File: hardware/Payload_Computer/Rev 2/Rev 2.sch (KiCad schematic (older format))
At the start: 0 parts

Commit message: Added Voltage Regulator
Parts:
- added H101: Center_Hole, Rev 2:Center_hole, symbol Rev2symbols:Center_Hole
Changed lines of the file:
@@
 $Descr A4 11693 8268
 encoding utf-8
-Sheet 1 2
+Sheet 1 3
 Title ""
 Date ""
@@
 F1 "TEENSY3.sch" 50
 $EndSheet
+$Comp
+L Rev2symbols:Center_Hole H101
+U 1 1 60565948
+P 5600 5650
+F 0 "H101" H 5678 5696 50  0000 L CNN
+F 1 "Center_Hole" H 5678 5605 50  0000 L CNN
+F 2 "Rev 2:Center_hole" H 5600 5650 50  0001 C CNN
+F 3 "" H 5600 5650 50  0001 C CNN
+	1    5600 5650
+	1    0    0    -1
+$EndComp
+$Sheet
+S 1050 900  1200 650
+U 60566AAD
+F0 "POWER REGULATION" 50
+F1 "POWER REGULATION.sch" 50
+$EndSheet
 $EndSCHEMATC

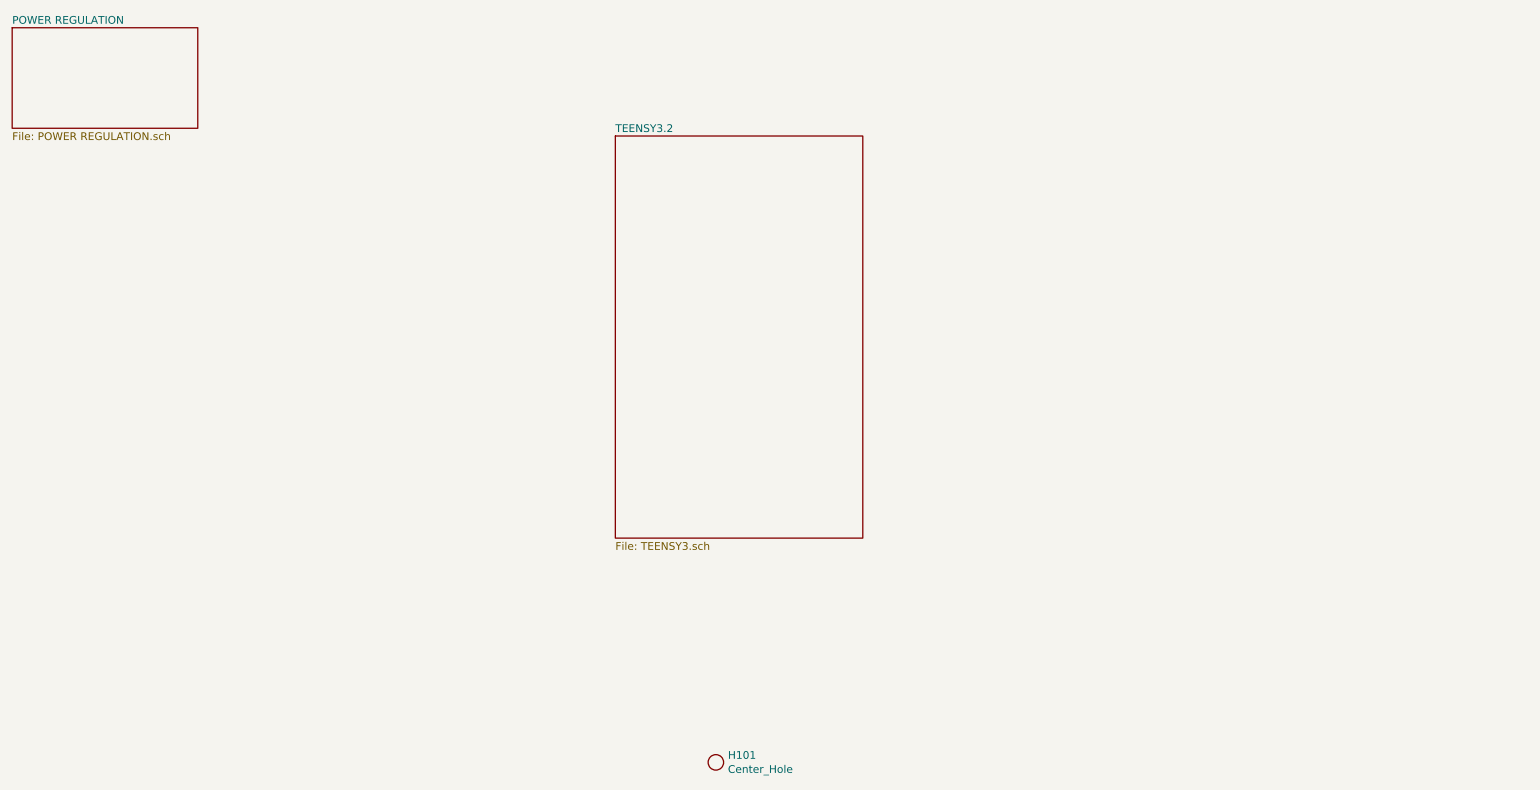
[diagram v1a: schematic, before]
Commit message: More routing and added BNO055
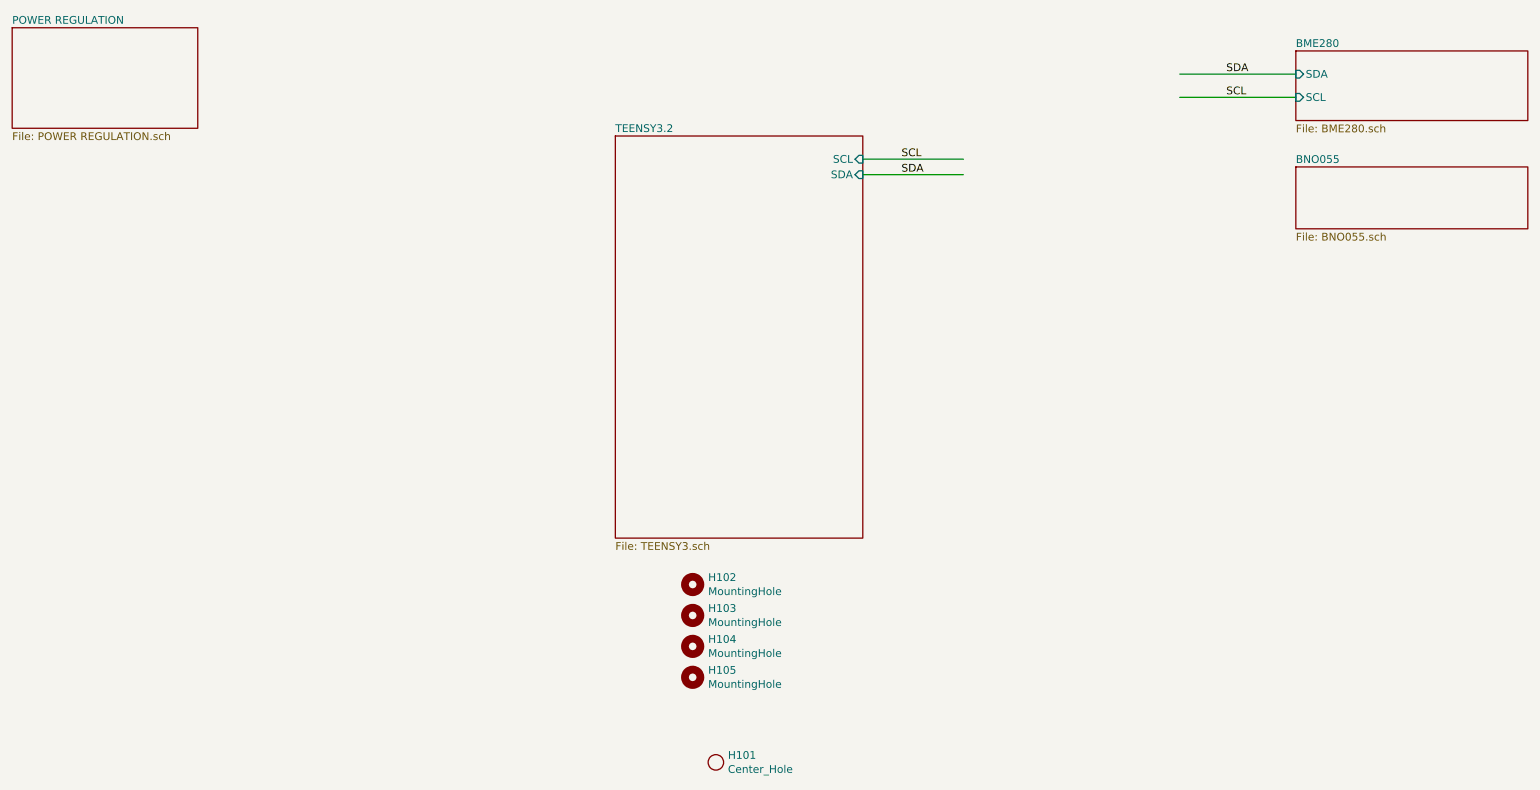
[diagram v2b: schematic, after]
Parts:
- added H102, H103, H104, H105: MountingHole, MountingHole:MountingHole_3.5mm, symbol Mechanical:MountingHole
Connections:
- net labels added: SCL, SDA
- wire segments 0 -> 4
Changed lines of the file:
@@
 $Descr A4 11693 8268
 encoding utf-8
-Sheet 1 3
+Sheet 1 5
 Title ""
 Date ""
@@
 F0 "TEENSY3.2" 50
 F1 "TEENSY3.sch" 50
+F2 "SCL" I R 6550 1750 50
+F3 "SDA" I R 6550 1850 50
 $EndSheet
 $Comp
@@
 F1 "POWER REGULATION.sch" 50
 $EndSheet
+$Sheet
+S 9350 1050 1500 450
+U 60605BA4
+F0 "BME280" 50
+F1 "BME280.sch" 50
+F2 "SDA" I L 9350 1200 50
+F3 "SCL" I L 9350 1350 50
+$EndSheet
+Wire Wire Line
+	9350 1200 8600 1200
+Wire Wire Line
+	9350 1350 8600 1350
+Text Label 8900 1200 0    50   ~ 0
+SDA
+Text Label 8900 1350 0    50   ~ 0
+SCL
+Wire Wire Line
+	6550 1750 7200 1750
+Wire Wire Line
+	6550 1850 7200 1850
+Text Label 6800 1750 0    50   ~ 0
+SCL
+Text Label 6800 1850 0    50   ~ 0
+SDA
+$Sheet
+S 9350 1800 1500 400
+U 6060BC6F
+F0 "BNO055" 50
+F1 "BNO055.sch" 50
+$EndSheet
+$Comp
+L Mechanical:MountingHole H105
+U 1 1 606125CD
+P 5450 5100
+F 0 "H105" H 5550 5146 50  0000 L CNN
+F 1 "MountingHole" H 5550 5055 50  0000 L CNN
+F 2 "MountingHole:MountingHole_3.5mm" H 5450 5100 50  0001 C CNN
+F 3 "~" H 5450 5100 50  0001 C CNN
+	1    5450 5100
+	1    0    0    -1
+$EndComp
+$Comp
+L Mechanical:MountingHole H104
+U 1 1 60612A94
+P 5450 4900
+F 0 "H104" H 5550 4946 50  0000 L CNN
+F 1 "MountingHole" H 5550 4855 50  0000 L CNN
+F 2 "MountingHole:MountingHole_3.5mm" H 5450 4900 50  0001 C CNN
+F 3 "~" H 5450 4900 50  0001 C CNN
+	1    5450 4900
+	1    0    0    -1
+$EndComp
+$Comp
+L Mechanical:MountingHole H103
+U 1 1 60612FC8
+P 5450 4700
+F 0 "H103" H 5550 4746 50  0000 L CNN
+F 1 "MountingHole" H 5550 4655 50  0000 L CNN
+F 2 "MountingHole:MountingHole_3.5mm" H 5450 4700 50  0001 C CNN
+F 3 "~" H 5450 4700 50  0001 C CNN
+	1    5450 4700
+	1    0    0    -1
+$EndComp
+$Comp
+L Mechanical:MountingHole H102
+U 1 1 6061316B
+P 5450 4500
+F 0 "H102" H 5550 4546 50  0000 L CNN
+F 1 "MountingHole" H 5550 4455 50  0000 L CNN
+F 2 "MountingHole:MountingHole_3.5mm" H 5450 4500 50  0001 C CNN
+F 3 "~" H 5450 4500 50  0001 C CNN
+	1    5450 4500
+	1    0    0    -1
+$EndComp
 $EndSCHEMATC

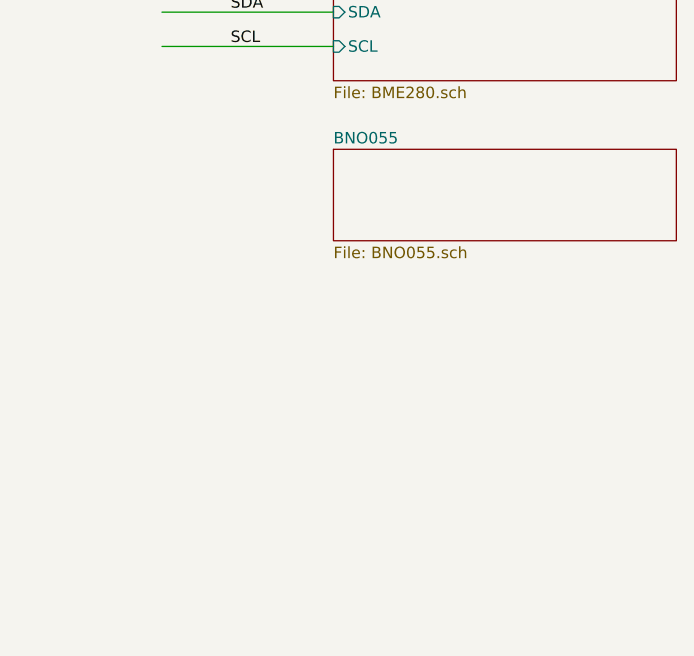
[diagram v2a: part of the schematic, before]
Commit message: Added SD card reader
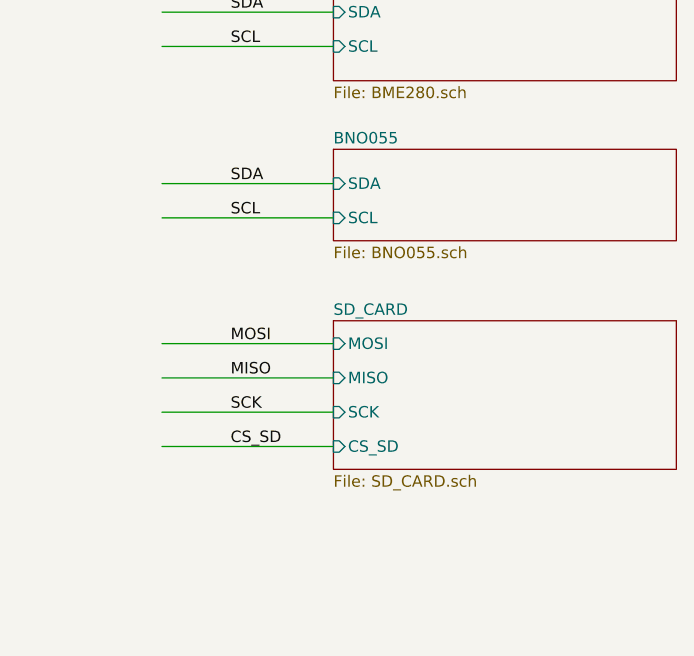
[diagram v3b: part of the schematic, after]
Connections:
- net labels added: CS_SD, MISO, MOSI, SCK
- wire segments 4 -> 10
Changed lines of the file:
@@
 $Descr A4 11693 8268
 encoding utf-8
-Sheet 1 5
+Sheet 1 6
 Title ""
 Date ""
@@
 F0 "BNO055" 50
 F1 "BNO055.sch" 50
+F2 "SCL" I L 9350 2100 50
+F3 "SDA" I L 9350 1950 50
 $EndSheet
 $Comp
@@
 	1    0    0    -1
 $EndComp
+Wire Wire Line
+	9350 1950 8600 1950
+Wire Wire Line
+	9350 2100 8600 2100
+Text Label 8900 1950 0    50   ~ 0
+SDA
+Text Label 8900 2100 0    50   ~ 0
+SCL
+$Sheet
+S 9350 2550 1500 650
+U 606A89B0
+F0 "SD_CARD" 50
+F1 "SD_CARD.sch" 50
+F2 "SCK" I L 9350 2950 50
+F3 "CS_SD" I L 9350 3100 50
+F4 "MOSI" I L 9350 2650 50
+F5 "MISO" I L 9350 2800 50
+$EndSheet
+Wire Wire Line
+	9350 2650 8600 2650
+Wire Wire Line
+	9350 2800 8600 2800
+Wire Wire Line
+	9350 2950 8600 2950
+Wire Wire Line
+	9350 3100 8600 3100
+Text Label 8900 3100 0    50   ~ 0
+CS_SD
+Text Label 8900 2950 0    50   ~ 0
+SCK
+Text Label 8900 2800 0    50   ~ 0
+MISO
+Text Label 8900 2650 0    50   ~ 0
+MOSI
 $EndSCHEMATC

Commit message: Did some stuff
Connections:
- net labels added: CS_FLASH
- wire segments 10 -> 17
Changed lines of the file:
@@
 $Descr A4 11693 8268
 encoding utf-8
-Sheet 1 6
+Sheet 1 7
 Title ""
 Date ""
@@
 F2 "SCL" I R 6550 1750 50
 F3 "SDA" I R 6550 1850 50
+F4 "SCK" I R 6550 2100 50
+F5 "MOSI" I R 6550 2200 50
+F6 "MISO" I R 6550 2300 50
 $EndSheet
 $Comp
@@
 Text Label 8900 2650 0    50   ~ 0
 MOSI
+$Sheet
+S 9350 3450 1500 650
+U 6068C99D
+F0 "FLASH CHIP" 50
+F1 "FLASH CHIP.sch" 50
+F2 "SCK" I L 9350 3850 50
+F3 "CS_FLASH" I L 9350 4000 50
+F4 "MISO" I L 9350 3700 50
+F5 "MOSI" I L 9350 3550 50
+$EndSheet
+Wire Wire Line
+	9350 3550 8600 3550
+Wire Wire Line
+	9350 3700 8600 3700
+Wire Wire Line
+	9350 3850 8600 3850
+Wire Wire Line
+	9350 4000 8600 4000
+Text Label 8900 3550 0    50   ~ 0
+MOSI
+Text Label 8900 3700 0    50   ~ 0
+MISO
+Text Label 8900 3850 0    50   ~ 0
+SCK
+Text Label 8900 4000 0    50   ~ 0
+CS_FLASH
+Wire Wire Line
+	6550 2100 7200 2100
+Wire Wire Line
+	6550 2200 7200 2200
+Wire Wire Line
+	6550 2300 7200 2300
+Text Label 6800 2100 0    50   ~ 0
+SCK
+Text Label 6800 2200 0    50   ~ 0
+MOSI
+Text Label 6800 2300 0    50   ~ 0
+MISO
 $EndSCHEMATC

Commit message: Finished some routing
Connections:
- wire segments 17 -> 19
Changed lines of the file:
@@
 F5 "MOSI" I R 6550 2200 50
 F6 "MISO" I R 6550 2300 50
+F7 "SD_CS" I R 6550 2500 50
+F8 "FLASH_CS" I R 6550 2600 50
 $EndSheet
 $Comp
@@
 Text Label 6800 2300 0    50   ~ 0
 MISO
+Wire Wire Line
+	6550 2500 7200 2500
+Wire Wire Line
+	6550 2600 7200 2600
+Text Label 6800 2500 0    50   ~ 0
+CS_SD
+Text Label 6750 2600 0    50   ~ 0
+CS_FLASH
 $EndSCHEMATC
